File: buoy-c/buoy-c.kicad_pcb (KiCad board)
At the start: 4 copper layers, 52.3 x 97.5 mm, 95 parts, among them J1 UJ31-CH-G2-SMT-TR, J10 Conn_01x06_Male, J11 TERM-BLK-2P, J14 Conn_01x09_Male, J2 BAT-HLD-001-THM, J3 Conn_01x02_Male, J4 U.FL-R-SMT-1_10_, J5 BH-18650-PC, J7 Conn_01x02_Male, J8 Conn_01x03_Male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

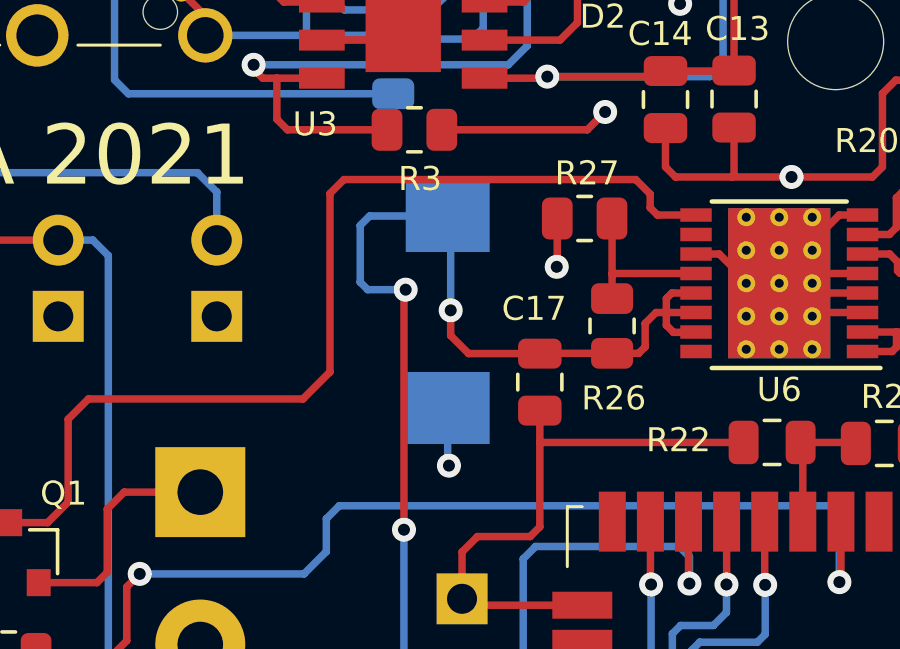
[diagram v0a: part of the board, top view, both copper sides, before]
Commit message: Added missing 3d Models
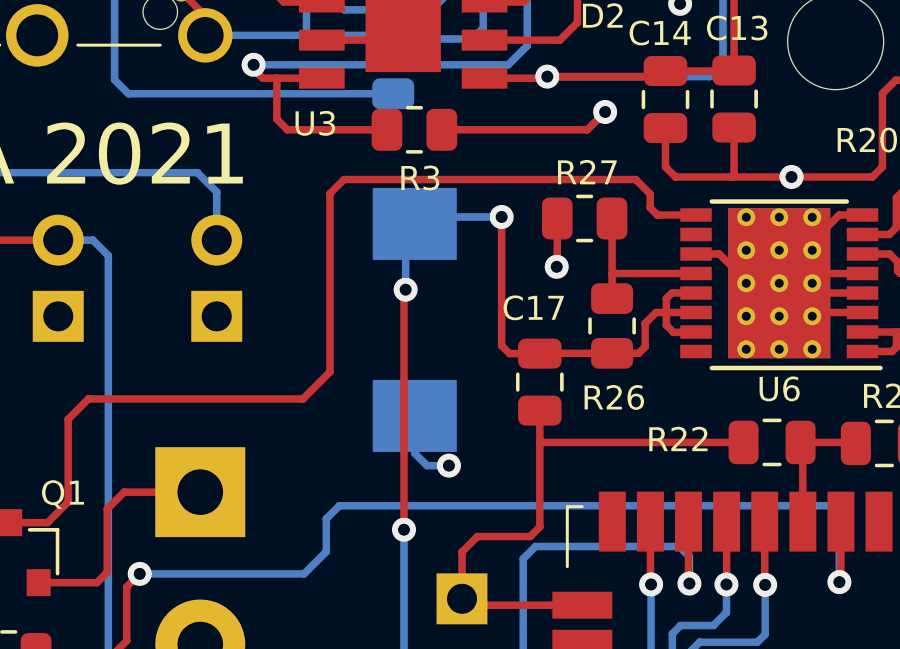
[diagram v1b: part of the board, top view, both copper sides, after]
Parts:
- moved C19 1.13 mm to (120.9, 132.3)
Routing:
- net +5V: track 58.8 -> 56.5 mm
- net GND: track 351.1 -> 351.8 mm
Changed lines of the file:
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@@
     (thickness 1.6)
     (drawings 43)
-    (tracks 1316)
+    (tracks 1317)
     (zones 0)
     (modules 95)
@@
     (0 F.Cu signal)
     (1 GND.Cu signal)
-    (2 Signal.Cu signal)
+    (2 Signal.Cu signal hide)
     (31 B.Cu signal)
     (32 B.Adhes user hide)
@@
   )
   (module C-2917-7343-Metric:C-2917-7343-Metric (layer B.Cu)
-    (at 122.04446 132.0419 270)
+    (at 120.94718 132.30606 270)
     (descr CY)
     (tags "Capacitor Polarised")
@@
       (rotate (xyz 0 0 0))
     )
+    (model ${KIPRJMOD}/3D/ECGSY0G471R.stp
+      (offset (xyz 22.75 2.25 -3))
+      (scale (xyz 1 1 1))
+      (rotate (xyz 0 0 0))
+    )
   )
   (module Capacitor_SMD:C_0805_2012Metric (layer B.Cu)
@@
       (rotate (xyz 0 0 0))
     )
+    (model ${KIPRJMOD}/3D/TP4056.stp
+      (at (xyz 0 0 0))
+      (scale (xyz 1 1 1))
+      (rotate (xyz 0 0 0))
+    )
   )
   (module Package_SO:TSSOP-28_4.4x9.7mm_P0.65mm (layer F.Cu)
@@
   (via (at 122.0851 137.16254) (size 0.8) (drill 0.4) (layers F.Cu B.Cu) (net 2))
   (segment (start 122.04446 137.1219) (end 122.0851 137.16254) (width 0.25) (layer B.Cu) (net 2))
-  (segment (start 122.04446 135.2419) (end 122.04446 137.1219) (width 0.25) (layer B.Cu) (net 2))
   (segment (start 118.13794 145.0721) (end 118.12778 145.06194) (width 0.25) (layer B.Cu) (net 2))
   (via (at 118.12778 145.06194) (size 0.8) (drill 0.4) (layers F.Cu B.Cu) (net 2))
@@
   (segment (start 119.82374 119.99392) (end 119.82374 118.364) (width 0.25) (layer F.Cu) (net 2))
   (segment (start 120.5611 120.73128) (end 119.82374 119.99392) (width 0.25) (layer F.Cu) (net 2))
+  (segment (start 122.0851 137.16254) (end 121.35612 137.16254) (width 0.25) (layer B.Cu) (net 2))
+  (segment (start 120.94718 136.7536) (end 120.94718 135.50606) (width 0.25) (layer B.Cu) (net 2))
+  (segment (start 121.35612 137.16254) (end 120.94718 136.7536) (width 0.25) (layer B.Cu) (net 2))
   (segment (start 108.82236 187.89266) (end 111.92236 187.89266) (width 0.25) (layer B.Cu) (net 3))
   (segment (start 111.92236 187.89266) (end 112.48012 187.89266) (width 0.25) (layer B.Cu) (net 3))
@@
   (segment (start 125.1248 133.41922) (end 125.11532 133.4287) (width 0.25) (layer F.Cu) (net 14))
   (segment (start 127.52324 133.41922) (end 125.1248 133.41922) (width 0.25) (layer F.Cu) (net 14))
-  (segment (start 125.11532 133.4287) (end 122.74292 133.4287) (width 0.25) (layer F.Cu) (net 14))
-  (via (at 122.14352 131.98602) (size 0.8) (drill 0.4) (layers F.Cu B.Cu) (net 14))
-  (segment (start 122.14352 132.8293) (end 122.14352 131.98602) (width 0.25) (layer F.Cu) (net 14))
-  (segment (start 122.74292 133.4287) (end 122.14352 132.8293) (width 0.25) (layer F.Cu) (net 14))
   (segment (start 122.14352 128.94096) (end 122.04446 128.8419) (width 0.25) (layer B.Cu) (net 14))
-  (segment (start 122.14352 131.98602) (end 122.14352 128.94096) (width 0.25) (layer B.Cu) (net 14))
+  (segment (start 125.11532 133.4287) (end 124.1069 133.4287) (width 0.25) (layer F.Cu) (net 14))
+  (via (at 123.84278 128.87452) (size 0.8) (drill 0.4) (layers F.Cu B.Cu) (net 14))
+  (segment (start 123.84278 133.16458) (end 123.84278 128.87452) (width 0.25) (layer F.Cu) (net 14))
+  (segment (start 124.1069 133.4287) (end 123.84278 133.16458) (width 0.25) (layer F.Cu) (net 14))
+  (segment (start 121.17872 128.87452) (end 120.94718 129.10606) (width 0.25) (layer B.Cu) (net 14))
+  (segment (start 123.84278 128.87452) (end 121.17872 128.87452) (width 0.25) (layer B.Cu) (net 14))
+  (via (at 120.64238 131.29768) (size 0.8) (drill 0.4) (layers F.Cu B.Cu) (net 14))
+  (via (at 120.5865 139.29868) (size 0.8) (drill 0.4) (layers F.Cu B.Cu) (net 14))
+  (segment (start 120.68302 128.8419) (end 120.94718 129.10606) (width 0.25) (layer B.Cu) (net 14))
+  (segment (start 118.7323 158.93034) (end 120.16486 158.93034) (width 0.25) (layer B.Cu) (net 14))
   (segment (start 122.52198 161.3662) (end 118.83136 161.3662) (width 0.25) (layer B.Cu) (net 14))
-  (segment (start 118.83136 161.3662) (end 118.33606 160.8709) (width 0.25) (layer B.Cu) (net 14))
   (segment (start 118.33606 160.8709) (end 118.33606 159.32658) (width 0.25) (layer B.Cu) (net 14))
   (segment (start 118.33606 159.32658) (end 118.7323 158.93034) (width 0.25) (layer B.Cu) (net 14))
-  (segment (start 118.7323 158.93034) (end 120.16486 158.93034) (width 0.25) (layer B.Cu) (net 14))
+  (segment (start 118.83136 161.3662) (end 118.33606 160.8709) (width 0.25) (layer B.Cu) (net 14))
   (segment (start 120.16486 158.93034) (end 120.5865 158.5087) (width 0.25) (layer B.Cu) (net 14))
-  (via (at 120.5865 139.29868) (size 0.8) (drill 0.4) (layers F.Cu B.Cu) (net 14))
-  (segment (start 120.5865 158.5087) (end 120.5865 139.29868) (width 0.25) (layer B.Cu) (net 14))
-  (via (at 120.64238 131.29768) (size 0.8) (drill 0.4) (layers F.Cu B.Cu) (net 14))
-  (segment (start 120.5865 131.35356) (end 120.64238 131.29768) (width 0.25) (layer F.Cu) (net 14))
   (segment (start 120.5865 139.29868) (end 120.5865 131.35356) (width 0.25) (layer F.Cu) (net 14))
-  (segment (start 120.64238 131.29768) (end 119.37746 131.29768) (width 0.25) (layer B.Cu) (net 14))
-  (segment (start 119.37746 131.29768) (end 119.126 131.04622) (width 0.25) (layer B.Cu) (net 14))
-  (segment (start 119.126 131.04622) (end 119.126 129.159) (width 0.25) (layer B.Cu) (net 14))
-  (segment (start 119.4431 128.8419) (end 122.04446 128.8419) (width 0.25) (layer B.Cu) (net 14))
-  (segment (start 119.126 129.159) (end 119.4431 128.8419) (width 0.25) (layer B.Cu) (net 14))
+  (segment (start 120.5865 131.35356) (end 120.64238 131.29768) (width 0.25) (layer F.Cu) (net 14))
+  (segment (start 120.5865 158.5087) (end 120.5865 139.29868) (width 0.25) (layer B.Cu) (net 14))
+  (segment (start 120.64238 129.41086) (end 120.94718 129.10606) (width 0.25) (layer B.Cu) (net 14))
+  (segment (start 120.64238 131.29768) (end 120.64238 129.41086) (width 0.25) (layer B.Cu) (net 14))
   (segment (start 126.74536 194.12458) (end 126.65964 194.2103) (width 0.25) (layer F.Cu) (net 15))
   (segment (start 128.67462 194.12458) (end 126.74536 194.12458) (width 0.25) (layer F.Cu) (net 15))

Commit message: Added gerber files
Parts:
- moved R33 1.28 mm to (141.2, 103.3)
- moved D2 1.10 mm to (127.2, 119.4)
- moved D1 0.97 mm to (127.2, 117.2)
- moved D4 0.89 mm to (150.1, 182.7)
- moved R30 0.89 mm to (150.1, 179.0)
- moved R14 0.72 mm to (140.9, 190.6)
- moved J5 0.58 mm to (135.0, 186.7)
- moved C10 0.58 mm to (123.0, 113.1)
- moved REF** 0.20 mm to (105.3, 193.5)
- moved REF** 0.20 mm to (105.3, 107.5)
- moved REF** 0.20 mm to (147.0, 193.5)
- moved REF** 0.20 mm to (147.0, 107.5)
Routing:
- net Net-(C4-Pad1): track 54.9 -> 49.4 mm
- net Net-(D1-Pad2): track 10.3 -> 7.36 mm
- net +BATT: track 232.6 -> 235.4 mm
- net Net-(R30-Pad1): track 8.39 -> 6.16 mm
- net /D+: track 124.1 -> 126.2 mm
- net Net-(D2-Pad2): track 13.7 -> 14.9 mm
- net Net-(D2-Pad1): track 5.27 -> 6.40 mm
- net GND: track 351.8 -> 352.8 mm
- net /5V_USB: track 208.6 -> 209.6 mm
- net Net-(R14-Pad2): track 7.12 -> 8.07 mm
- net Net-(D1-Pad1): track 6.16 -> 7.10 mm
- net VDD: track 183.5 -> 182.7 mm, vias 6 -> 8
- net BAT-CR2032: track 83.0 -> 83.7 mm
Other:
- board size 52.3 x 97.5 mm -> 51.2 x 97.5 mm
- board text added: "EJA M v1.0"
- board text added: "Hackaday Dream Team 2021 EJA M v1.0 02-Sep-2021"
- board text removed: "EJA 2021"

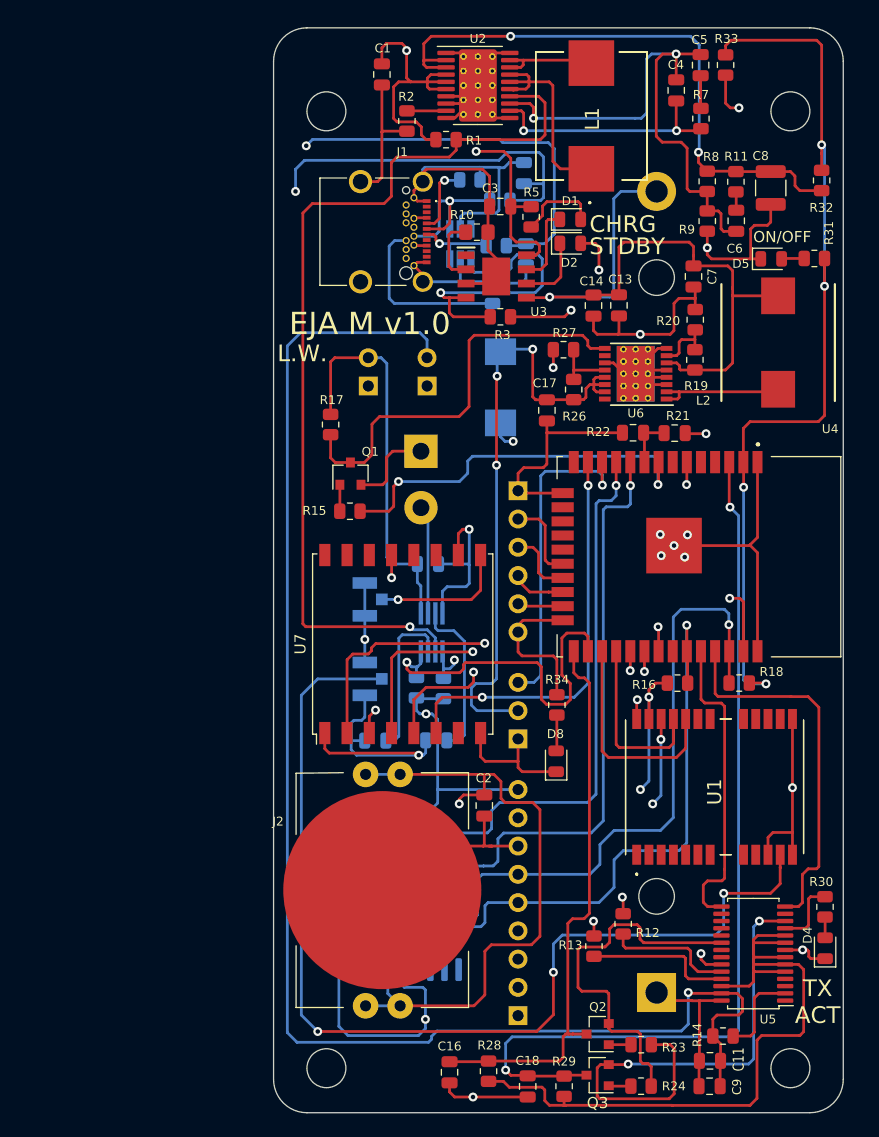
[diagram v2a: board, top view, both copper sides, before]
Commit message: Removed FTDI and added extra headers
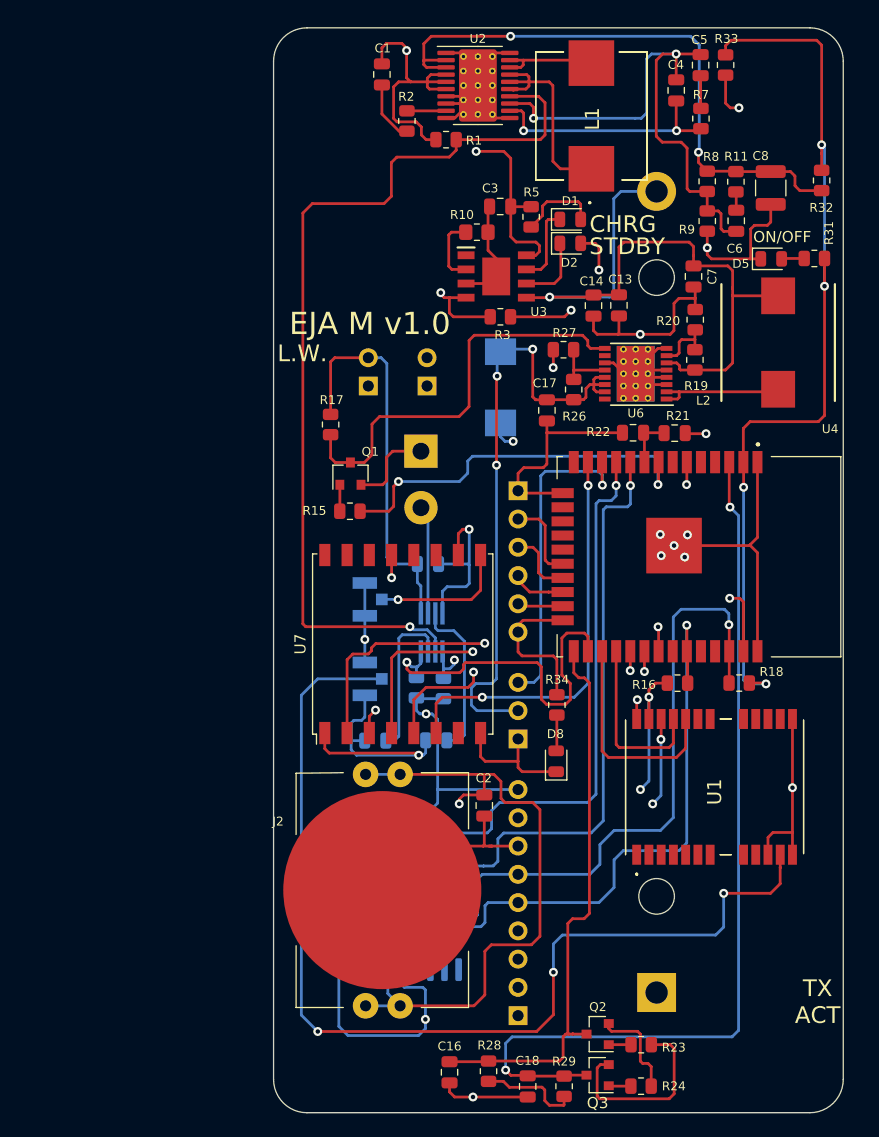
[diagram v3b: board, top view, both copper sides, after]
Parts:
- removed C10, C12: 47pF, Capacitor_SMD:C_0805_2012Metric
- removed C11: 4.7uF, Capacitor_SMD:C_0805_2012Metric
- removed C9: 100nF, Capacitor_SMD:C_0805_2012Metric
- removed D3: CPDT6-5V4-HF, Package_TO_SOT_SMD:SOT-23-6_Handsoldering
- removed D4: RED-CLEAR, LED_SMD:LED_0805_2012Metric
- removed FB1, FB2: 350m, Resistor_SMD:R_0805_2012Metric
- removed J1: UJ31-CH-G2-SMT-TR, UJ31CHG2SMTTR:UJ31CHG2SMTTR
- removed R12, R13: 27, Resistor_SMD:R_0805_2012Metric
- removed R14, R4, R6: 5.1k, Resistor_SMD:R_0805_2012Metric
- removed R30: 620, Resistor_SMD:R_0805_2012Metric
- removed REF** (x4): MountingHole_3.5mm, MountingHole:MountingHole_3.5mm
- removed U5: FT260S-U, Package_SO:TSSOP-28_4.4x9.7mm_P0.65mm
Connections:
- net 3V3_FTDI renamed Net-(J1-Pad6)
- J14 pad 1: Net-(J14-Pad1) -> (no net)
- J14 pad 2: Net-(J14-Pad2) -> (no net)
- J14 pad 3: Net-(J14-Pad3) -> (no net)
- J14 pad 4: Net-(J14-Pad4) -> (no net)
- J14 pad 8: Net-(J14-Pad8) -> (no net)
- U1 pad 1: Net-(U1-Pad1) -> (no net)
- U1 pad 14: Net-(U1-Pad14) -> (no net)
- U1 pad 15: Net-(U1-Pad15) -> (no net)
- U1 pad 16: Net-(U1-Pad16) -> (no net)
- U1 pad 17: Net-(U1-Pad17) -> (no net)
- U1 pad 18: Net-(U1-Pad18) -> (no net)
- U1 pad 19: Net-(U1-Pad19) -> (no net)
- U1 pad 2: Net-(U1-Pad2) -> (no net)
- U1 pad 3: Net-(U1-Pad3) -> (no net)
- U1 pad 4: Net-(U1-Pad4) -> (no net)
- U1 pad 5: Net-(U1-Pad5) -> (no net)
- U1 pad 6: Net-(U1-Pad6) -> (no net)
- U1 pad 7: Net-(U1-Pad7) -> (no net)
- U1 pad 8: Net-(U1-Pad8) -> (no net)
- U1 pad 9: Net-(U1-Pad9) -> (no net)
- U3 pad 1: Net-(U3-Pad1) -> (no net)
- U4 pad 14: Net-(U4-Pad14) -> (no net)
- U4 pad 16: Net-(U4-Pad16) -> (no net)
- U4 pad 17: Net-(U4-Pad17) -> (no net)
- U4 pad 18: Net-(U4-Pad18) -> (no net)
- U4 pad 19: Net-(U4-Pad19) -> (no net)
- U4 pad 32: Net-(U4-Pad32) -> (no net)
- U4 pad 4: Net-(U4-Pad4) -> (no net)
- U4 pad 5: Net-(U4-Pad5) -> (no net)
- U4 pad 7: Net-(U4-Pad7) -> (no net)
- U6 pad 10: Net-(U6-Pad10) -> (no net)
- U6 pad 16: Net-(U6-Pad16) -> (no net)
- U7 pad 11: Net-(U7-Pad11) -> (no net)
- U7 pad 12: Net-(U7-Pad12) -> (no net)
- U7 pad 14: Net-(U7-Pad14) -> (no net)
- U7 pad 15: Net-(U7-Pad15) -> (no net)
- U7 pad 16: Net-(U7-Pad16) -> (no net)
- U7 pad 7: Net-(U7-Pad7) -> (no net)
- U8 pad 1: Net-(U8-Pad1) -> (no net)
- U8 pad 10: Net-(U8-Pad10) -> (no net)
- U8 pad 11: Net-(U8-Pad11) -> (no net)
- U8 pad 12: Net-(U8-Pad12) -> (no net)
- U8 pad 5: Net-(U8-Pad5) -> (no net)
- U8 pad 6: Net-(U8-Pad6) -> (no net)
- U8 pad 7: Net-(U8-Pad7) -> (no net)
- U8 pad 8: Net-(U8-Pad8) -> (no net)
- U8 pad 9: Net-(U8-Pad9) -> (no net)
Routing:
- net /5V_USB: track 209.6 -> 54.6 mm, vias 3 -> 2
- net /D-: track 131.3 -> 0.00 mm, vias 2 -> 0
- net /D+: track 126.2 -> 0.00 mm, vias 2 -> 0
- net GND: track 352.8 -> 275.9 mm, vias 18 -> 16
- net Net-(J1-Pad6): track 65.1 -> 9.04 mm
- net ESP_TX: track 34.0 -> 0.00 mm
- net /RTS: track 45.3 -> 17.2 mm, vias 2 -> 0
- net ESP_RX: track 27.6 -> 0.00 mm
- net /DTR: track 33.8 -> 8.87 mm
- net /FB2: track 16.5 -> 0.00 mm, vias 1 -> 0
- net Net-(J1-PadB5): track 15.9 -> 0.00 mm
- net Net-(R13-Pad1): track 13.2 -> 0.00 mm
- net Net-(R12-Pad1): track 11.6 -> 0.00 mm
- net Net-(R14-Pad2): track 8.07 -> 0.00 mm
- net /FB1: track 30.2 -> 22.9 mm, vias 1 -> 0
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
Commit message: Re routed Sepic converter
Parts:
- removed J14: Conn_01x09_Male, Connector_PinHeader_2.54mm:PinHeader_1x09_P2.54mm_Vertical
- removed R33: 0, Resistor_SMD:R_0805_2012Metric
- added J1: Conn_01x06_Male, Connector_PinHeader_2.54mm:PinHeader_1x06_P2.54mm_Vertical, F.Cu at (79.4, 103.0)
- added J12: Conn_01x04_Male, Connector_PinHeader_2.54mm:PinHeader_1x04_P2.54mm_Vertical, F.Cu at (90.1, 108.0)
- added J6: Conn_01x06_Male, Connector_PinHeader_2.54mm:PinHeader_1x06_P2.54mm_Vertical, F.Cu at (84.0, 103.0)
- added R4: 100k, Resistor_SMD:R_0805_2012Metric_Pad1.20x1.40mm_HandSolder, F.Cu at (88.7, 102.2)
- added R6: 100k, Resistor_SMD:R_0805_2012Metric_Pad1.20x1.40mm_HandSolder, F.Cu at (93.5, 102.2)
- C19: moved to F.Cu
- moved C1 25.9 mm to (136.1, 106.4), turned to 90 degrees
- moved R1 22.2 mm to (138.2, 108.8), turned to 90 degrees
- moved R2 21.0 mm to (133.4, 106.4), turned to 90 degrees
- moved L1 16.2 mm to (113.0, 108.5), turned to 270 degrees
- moved C5 14.2 mm to (124.8, 102.3), turned to 0 degrees
- moved R7 10.9 mm to (129.7, 102.3), turned to 0 degrees
- moved C4 9.75 mm to (127.1, 104.5), turned to 0 degrees
- moved U2 9.23 mm to (127.0, 109.6), turned to 180 degrees
- moved D2 4.94 mm to (126.7, 124.3), turned to 270 degrees
- moved R32 1.35 mm to (148.5, 113.8), turned to 90 degrees
- moved C19 1.24 mm to (120.6, 133.5), turned to 90 degrees
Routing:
- net +BATT: track 235.4 -> 132.7 mm, vias 4 -> 1
- net +3V3: track 54.6 -> 13.5 mm, vias 2 -> 0
- net VDD: track 182.7 -> 148.3 mm, vias 8 -> 6
- net Net-(C4-Pad1): track 49.4 -> 17.3 mm, vias 2 -> 0
- net /FB1: track 22.9 -> 0.00 mm
- net /5V_USB: track 54.6 -> 40.8 mm, vias 2 -> 0
- net +5V: track 56.5 -> 46.5 mm, vias 3 -> 1
- net Net-(D2-Pad2): track 14.9 -> 5.13 mm, vias 2 -> 0
- net Net-(C4-Pad2): track 21.6 -> 16.1 mm, vias 2 -> 0
- net Net-(L1-Pad2): track 9.18 -> 13.6 mm
- net EN_3V3: track 83.9 -> 80.3 mm
- net Net-(D2-Pad1): track 6.40 -> 3.54 mm
- net GND: track 275.9 -> 278.5 mm
- net Net-(L1-Pad1): track 19.4 -> 18.6 mm
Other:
- board text removed: "TX ACT"
